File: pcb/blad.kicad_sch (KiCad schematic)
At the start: 91 parts, among them J1 Conn_01x04, J2 Conn_01x02_Pin, SW1 1U, SW10 1U, SW11 1U, SW12 1U, SW13 1.25U, SW14 1U, SW15 1U, SW16 1U, SW17 1U, SW18 1U, SW19 1U, SW2 1U, SW20 1U, SW21 1U, SW22 1U, SW23 1.75U, SW24 1U, SW25 1U, SW26 1U, SW27 1U, SW28 1U, SW29 1U, SW3 1U, SW30 1U, SW31 1U, SW32 1U, SW33 1.25U, SW34 1.25U, SW35 1U, SW36 1.25U, SW37 2.75U, SW38 1.25U, SW39 1U, SW4 1U, SW40 1.25U, SW41 1.75U, SW42 2.25U, SW5 1U, SW6 1U, SW7 1U, SW8 1U, SW9 1U, U1 HY0020

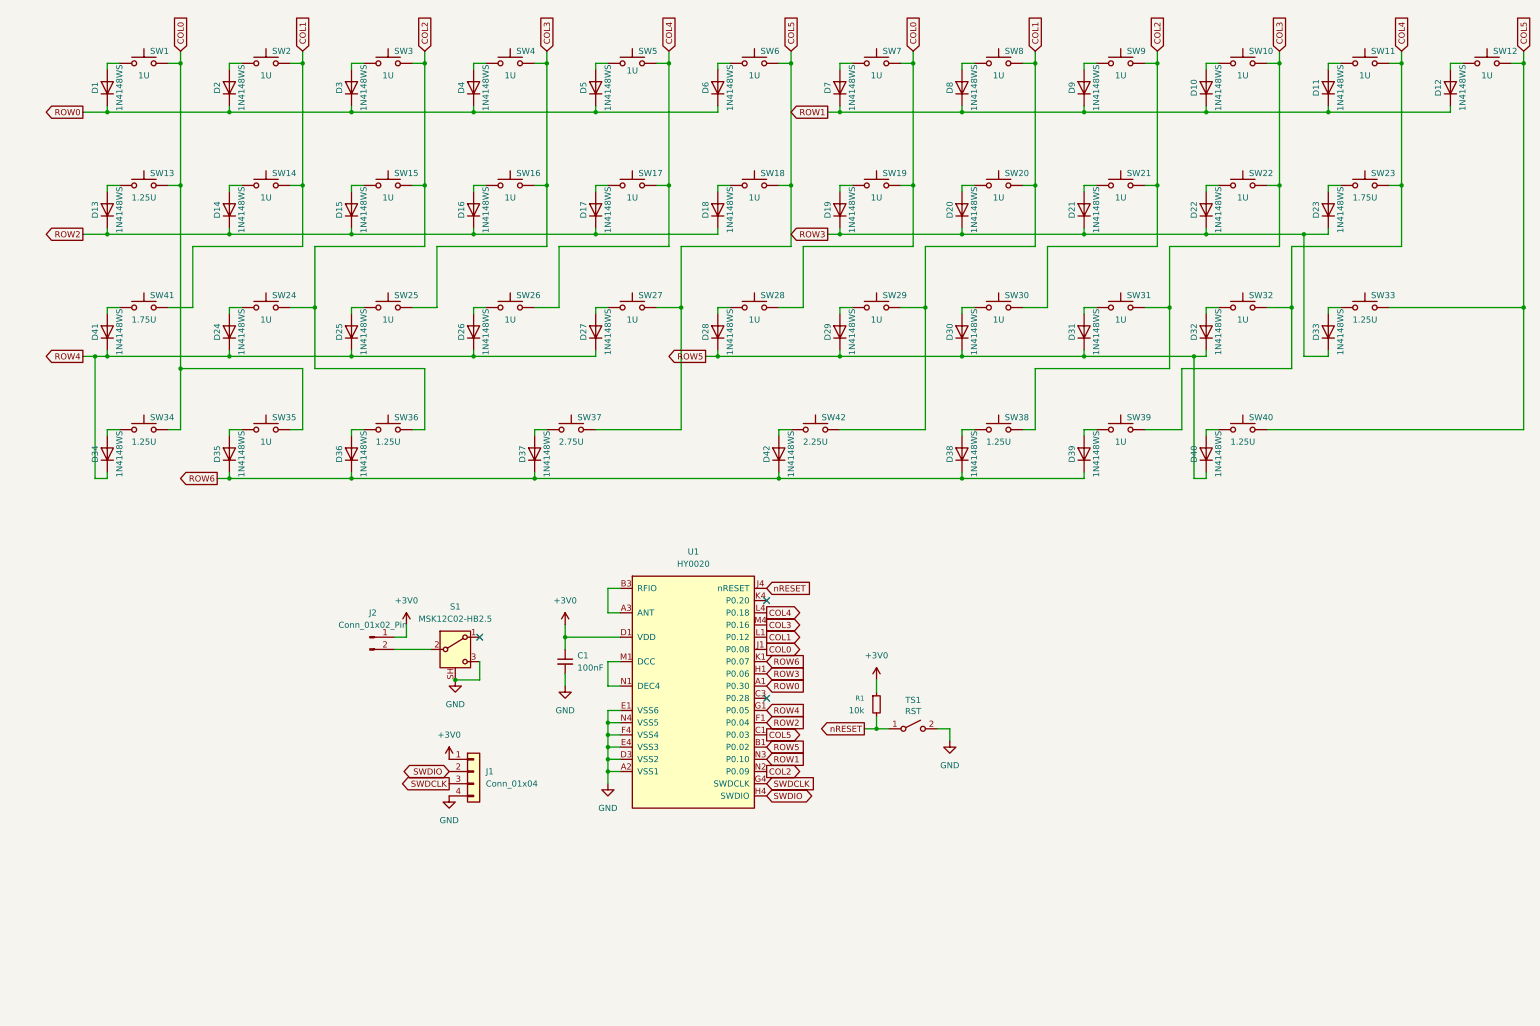
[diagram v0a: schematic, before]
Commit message: Migrate PCB to MS88SF21 module
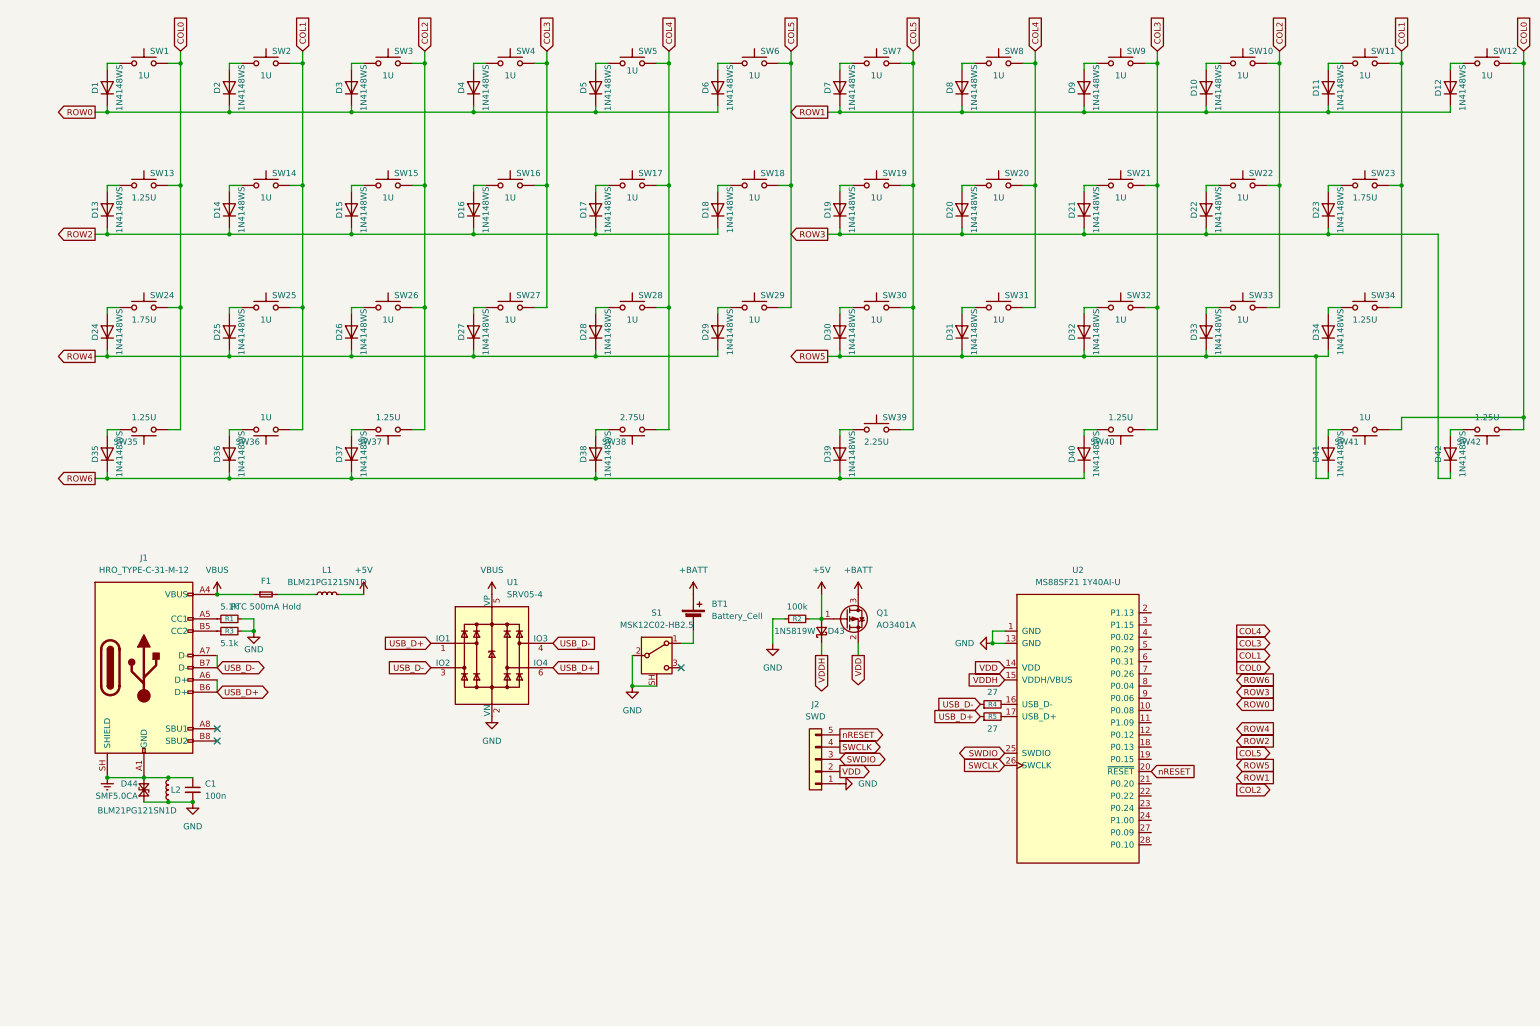
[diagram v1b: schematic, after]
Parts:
- removed J1: Conn_01x04, Connector_PinHeader_2.54mm:PinHeader_1x04_P2.54mm_Vertical, symbol Connector_Generic:Conn_01x04
- removed J2: Conn_01x02_Pin, Connector_PinHeader_2.54mm:PinHeader_1x02_P2.54mm_Vertical, symbol Connector:Conn_01x02_Pin
- removed TS1: RST, Button_Switch_SMD:SW_Push_SPST_NO_Alps_SKRK, symbol Switch:SW_SPST
- removed U1: HY0020, Smidr:RF_Module_FDK_HY0020, symbol Smidr:FDK_HY0020
- added BT1: Battery_Cell, Smidr:BatteryHolder_Takachi_BS-S-1632, symbol Device:Battery_Cell
- added D43: 1N5819W, Diode_SMD:D_SOD-123, symbol Device:D_Schottky_Small
- added D44: SMF5.0CA, Diode_SMD:D_SOD-123F, symbol Device:D_TVS_Small
- added F1: PTC 500mA Hold, Fuse:Fuse_1206_3216Metric, symbol Device:Fuse_Small
- added J1: HRO_TYPE-C-31-M-12, Connector_USB:USB_C_Receptacle_HRO_TYPE-C-31-M-12, symbol Connector:USB_C_Receptacle_USB2.0_16P
- added J2: SWD, Connector_PinHeader_1.00mm:PinHeader_1x05_P1.00mm_Vertical, symbol Connector_Generic:Conn_01x05
- added L1, L2: BLM21PG121SN1D, Inductor_SMD:L_0805_2012Metric, symbol Device:L_Small
- added Q1: AO3401A, Package_TO_SOT_SMD:SOT-23, symbol Transistor_FET:AO3401A
- added R2: 100k, Resistor_SMD:R_0603_1608Metric, symbol Device:R_Small
- added R3: 5.1k, Resistor_SMD:R_0603_1608Metric, symbol Device:R_Small
- added R4, R5: 27, Resistor_SMD:R_0603_1608Metric, symbol Device:R_Small
- added U1: SRV05-4, Package_TO_SOT_SMD:SOT-23-6, symbol Power_Protection:SRV05-4
- added U2: MS88SF21 1Y40AI-U, Smidr:RF_Module_MinewSemi_MS88SF21, symbol Smidr:MinewSemi_MS88SF21_1Y40AI_U
- C1: value 100nF -> 100n; footprint Capacitor_SMD:C_0402_1005Metric -> Capacitor_SMD:C_0603_1608Metric; JLCPCB Part # (none) -> C14663
- R1: value 10k -> 5.1k; footprint Resistor_SMD:R_0402_1005Metric -> Resistor_SMD:R_0603_1608Metric; JLCPCB Part # (none) -> C23186
- renumbered D41 to D24, D24 to D25, D25 to D26, D26 to D27, D27 to D28, D28 to D29, D29 to D30, D30 to D31, D31 to D32, D32 to D33, D33 to D34, D34 to D35, D35 to D36, D36 to D37, D37 to D38, D42 to D39, D38 to D40, D39 to D41, D40 to D42, SW41 to SW24, SW24 to SW25, SW25 to SW26, SW26 to SW27, SW27 to SW28, SW28 to SW29, SW29 to SW30, SW30 to SW31, SW31 to SW32, SW32 to SW33, SW33 to SW34, SW34 to SW35, SW35 to SW36, SW36 to SW37, SW37 to SW38, SW42 to SW39, SW38 to SW40, SW39 to SW41, SW40 to SW42
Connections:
- net COL0: now also SW12.2, SW24.2, SW35.1, SW41.1, SW42.1; no longer SW19.2, SW29.2, SW35.2, SW36.2, SW7.2
- net COL1: now also SW11.2, SW23.2, SW25.2, SW34.2, SW36.1; no longer SW20.2, SW24.2, SW30.2, SW39.2, SW8.2
- net COL2: now also SW10.2, SW22.2, SW26.2, SW33.2, SW37.1; no longer SW21.2, SW25.2, SW31.2, SW37.2, SW9.2
- net COL3: now also SW21.2, SW27.2, SW40.1, SW9.2; no longer SW10.2, SW22.2, SW26.2, SW40.2
- net COL4: now also SW20.2, SW28.2, SW31.2, SW38.1, SW8.2; no longer SW11.2, SW23.2, SW27.2, SW33.2, SW41.2
- net COL5: now also SW19.2, SW29.2, SW30.2, SW39.2, SW7.2; no longer SW12.2, SW28.2, SW34.2, SW38.2, SW42.2
- net GND: now also R1.2, S1.2 (B), D44.1 (A1), J2.1 (Pin_1), L2.1, R2.1, R3.2, U1.2 (VN), U2.1 (GND), U2.13 (GND); no longer S1.3 (C)
- net ROW3: now also D42.1 (K); no longer D34.1 (K)
- net ROW4: now also D29.1 (K); no longer D35.1 (K)
- net ROW5: now also D34.1 (K), D41.1 (K); no longer D29.1 (K), D42.1 (K)
- net ROW6: now also D35.1 (K); no longer D41.1 (K)
- net SWDIO: now also J2.3 (Pin_3), U2.25 (SWDIO)
- net nRESET: now also J2.5 (Pin_5), U2.20 (P0.18); no longer R1.2
- net at D41.2 (A): now also SW41.2; no longer SW41.1
- net at D42.2 (A): now also SW42.2; no longer SW42.1
- net at D36.2 (A): now also SW36.2; no longer SW36.1
- net at D37.2 (A): now also SW37.2; no longer SW37.1
- net at D38.2 (A): now also SW38.2; no longer SW38.1
- net at D40.2 (A): now also SW40.2; no longer SW40.1
- net at D35.2 (A): now also SW35.2; no longer SW35.1
- net at S1.1 (A): now also BT1.2 (-)
- net +3V0: no longer names the net of R1.1
- net +3V0: now also J1.A5 (CC1); no longer C1.1
- new net: F1.2, L1.1
- new net: R5.2, U2.17 (USB_D+)
- new net: J1.B5 (CC2), R3.1
- new net: R4.2, U2.16 (USB_D-)
- new net +5V: D43.2 (A), L1.2, Q1.1 (G), R2.2
- new net +BATT: BT1.1 (+), Q1.3 (D)
- new net Earth: C1.1, D44.2 (A2), J1.A1 (GND), J1.A12 (GND), J1.B1 (GND), J1.B12 (GND), J1.SH (SHIELD), L2.2
- new net SWCLK: J2.4 (Pin_4), U2.26 (SWCLK)
- new net USB_D+: J1.A6 (D+), J1.B6 (D+), R5.1, U1.1 (IO1), U1.6 (IO4)
- new net USB_D-: J1.A7 (D-), J1.B7 (D-), R4.1, U1.3 (IO2), U1.4 (IO3)
- new net VBUS: F1.1, J1.A4 (VBUS), J1.A9 (VBUS), J1.B4 (VBUS), J1.B9 (VBUS), U1.5 (VP)
- new net VDD: J2.2 (Pin_2), Q1.2 (S), U2.14 (VDD)
- new net VDDH: D43.1 (K), U2.15 (VDDH/VBUS)
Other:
- moved on the sheet: D38, D39, D40, D41, D42, S1, SW35, SW36, SW37, SW38, SW39, SW40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

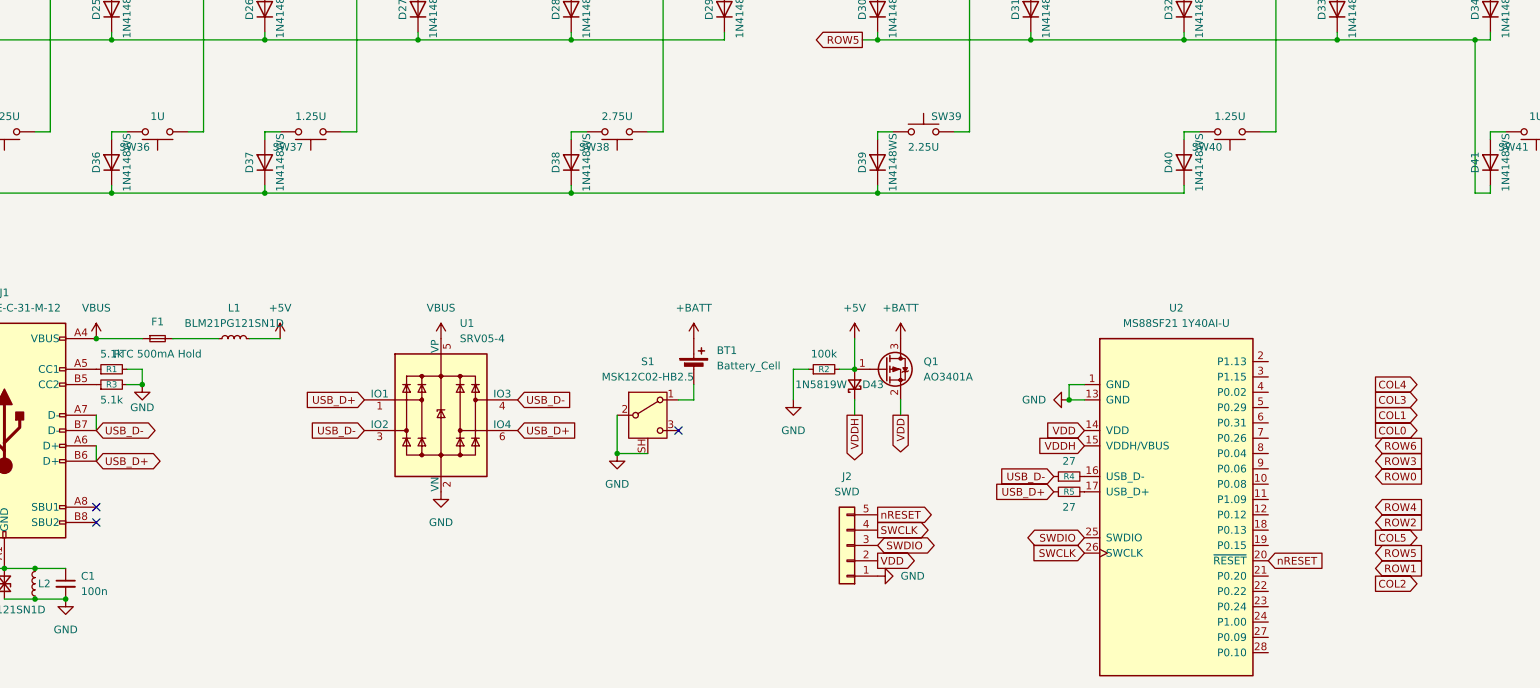
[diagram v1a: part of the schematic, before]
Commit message: Update PCB power wiring and stabilizer cutouts
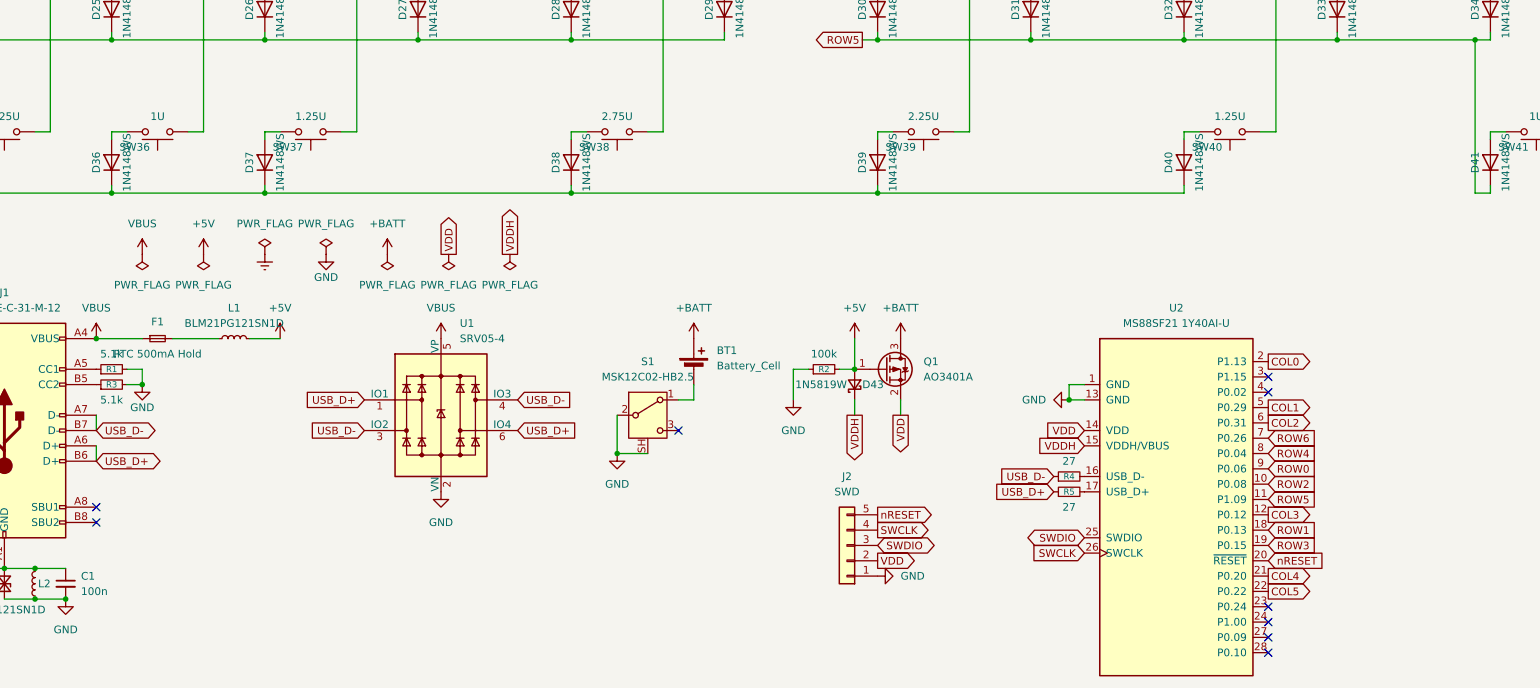
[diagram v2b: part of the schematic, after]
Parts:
- S1: symbol local:SW_SPDT_Shielded -> Smidr:SW_SPDT_Shielded
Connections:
- net COL0: now also U2.2 (P1.13)
- net COL1: now also U2.5 (P0.29)
- net COL2: now also U2.6 (P0.31)
- net COL3: now also U2.12 (P0.12)
- net COL4: now also U2.21 (P0.20)
- net COL5: now also SW39.1, U2.22 (P0.22); no longer SW39.2
- net ROW0: now also U2.9 (P0.06)
- net ROW1: now also U2.18 (P0.13)
- net ROW2: now also U2.10 (P0.08)
- net ROW3: now also U2.19 (P0.15)
- net ROW4: now also U2.8 (P0.04)
- net ROW5: now also U2.11 (P1.09)
- net ROW6: now also U2.7 (P0.26)
- net at D39.2 (A): now also SW39.2; no longer SW39.1
- no-connect marks 3 -> 9
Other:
- moved on the sheet: SW39

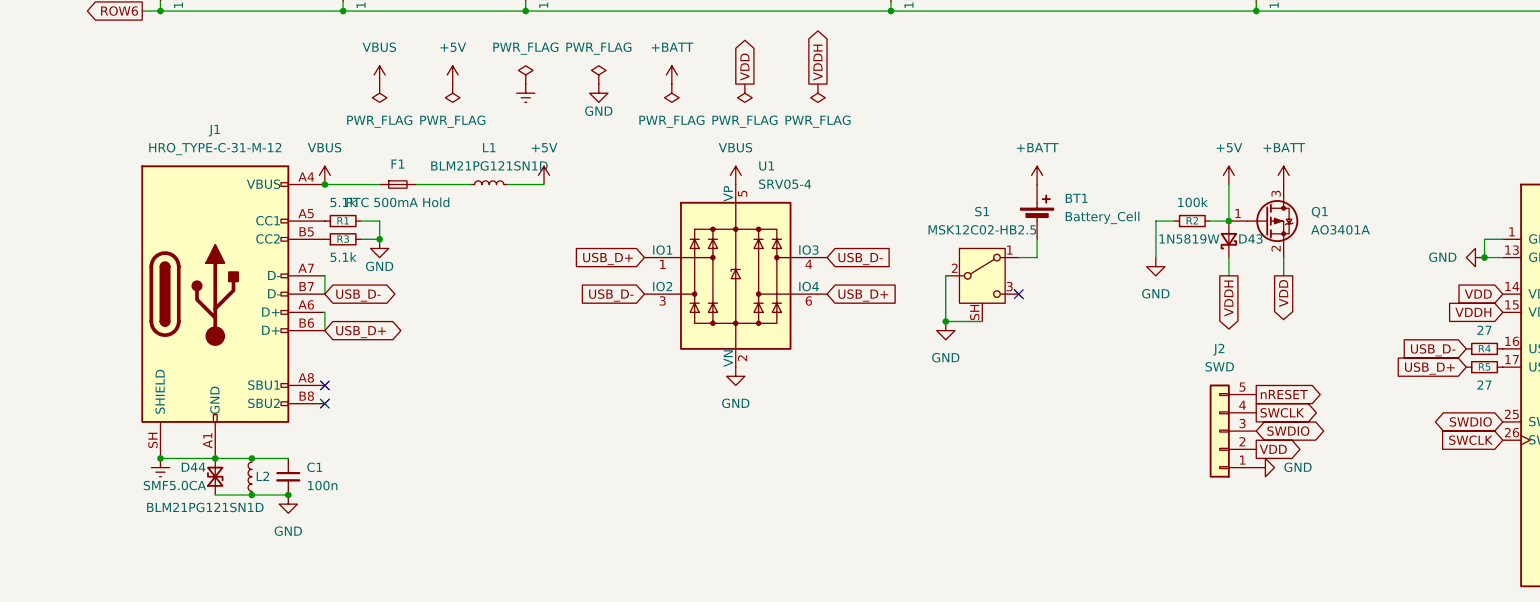
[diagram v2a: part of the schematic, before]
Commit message: Fix USB grounding and add battery bulk capacitor
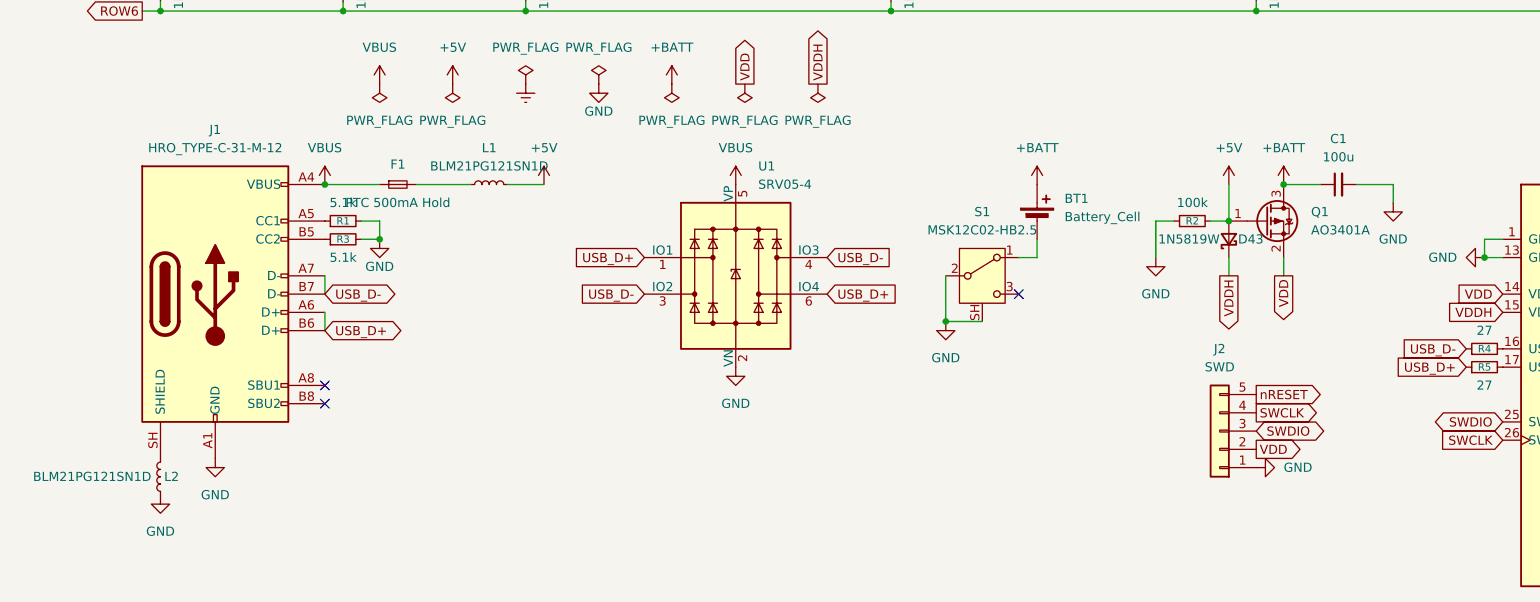
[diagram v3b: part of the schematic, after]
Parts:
- removed D44: SMF5.0CA, Diode_SMD:D_SOD-123F, symbol Device:D_TVS_Small
- C1: value 100n -> 100u; footprint Capacitor_SMD:C_0603_1608Metric -> Capacitor_SMD:C_1206_3216Metric; JLCPCB Part # C14663 -> C15008
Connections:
- net +BATT: now also C1.1
- net Earth: no longer C1.1, J1.A1 (GND), J1.A12 (GND), J1.B1 (GND), J1.B12 (GND), J1.SH (SHIELD), L2.2
- net GND: now also J1.A1 (GND), J1.A12 (GND), J1.B1 (GND), J1.B12 (GND)
- new net: J1.SH (SHIELD), L2.2
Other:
- moved on the sheet: L2

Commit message: Add mounting holes and update case geometry
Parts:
- added H1, H10, H11, H12, H13, H2, H3, H4, H5, H6, H7, H8, H9: MountingHole, MountingHole:MountingHole_2.1mm, symbol Mechanical:MountingHole
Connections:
- net at BT1.2 (-): now also S1.3 (C); no longer S1.1 (A)

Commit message: Update PCB routing and schematic connectivity
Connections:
- net COL0: now also SW35.2, SW41.2, SW42.2, U2.9 (P0.06); no longer SW35.1, SW41.1, SW42.1, U2.2 (P1.13)
- net COL1: now also SW36.2, U2.8 (P0.04); no longer SW36.1, U2.5 (P0.29)
- net COL2: now also U2.12 (P0.12); no longer U2.6 (P0.31)
- net COL3: now also SW40.2, U2.27 (P0.09); no longer SW40.1, U2.12 (P0.12)
- net COL5: now also U2.23 (P0.24); no longer U2.22 (P0.22)
- net ROW0: now also U2.10 (P0.08); no longer U2.9 (P0.06)
- net ROW1: now also U2.22 (P0.22); no longer U2.18 (P0.13)
- net ROW2: now also U2.11 (P1.09); no longer U2.10 (P0.08)
- net ROW4: now also U2.28 (P0.10); no longer U2.8 (P0.04)
- net ROW5: now also U2.18 (P0.13); no longer U2.11 (P1.09)
- net ROW6: now also U2.24 (P1.00); no longer U2.7 (P0.26)
- net USB_D+: now also U1.3 (IO2); no longer U1.1 (IO1), U1.6 (IO4)
- net USB_D-: now also U1.1 (IO1); no longer U1.3 (IO2), U1.4 (IO3)
- net at D41.2 (A): now also SW41.1; no longer SW41.2
- net at D42.2 (A): now also SW42.1; no longer SW42.2
- net at D36.2 (A): now also SW36.1; no longer SW36.2
- net at D40.2 (A): now also SW40.1; no longer SW40.2
- net at D35.2 (A): now also SW35.1; no longer SW35.2
- net DP: now reaches R5.2, U2.17 (USB_D+)
- net DN: now reaches R4.2, U2.16 (USB_D-)
- no-connect marks 9 -> 11
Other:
- moved on the sheet: R4, R5, SW35, SW36, SW40, SW41, SW42
